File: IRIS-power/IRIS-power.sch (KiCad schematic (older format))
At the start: 11 parts, among them J101 Powerpole, J102 PJ-047AH, U101 TVS1400DRV, U102 TVS1400DRV

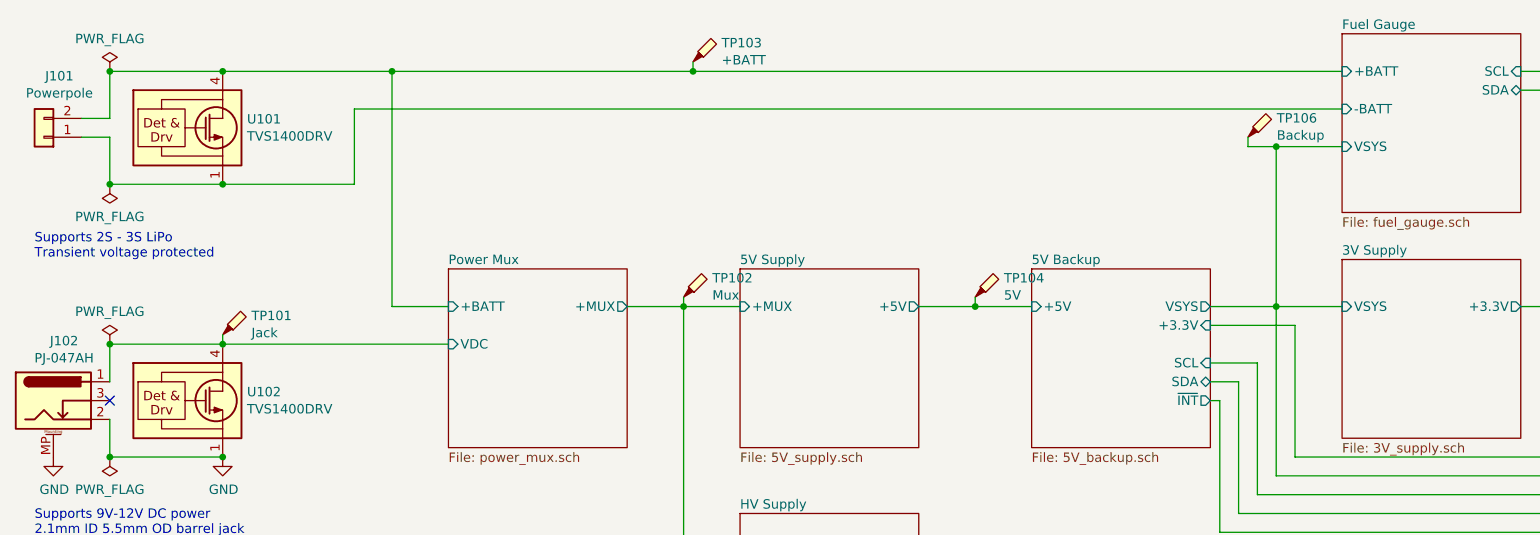
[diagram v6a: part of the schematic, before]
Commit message: Updated layout
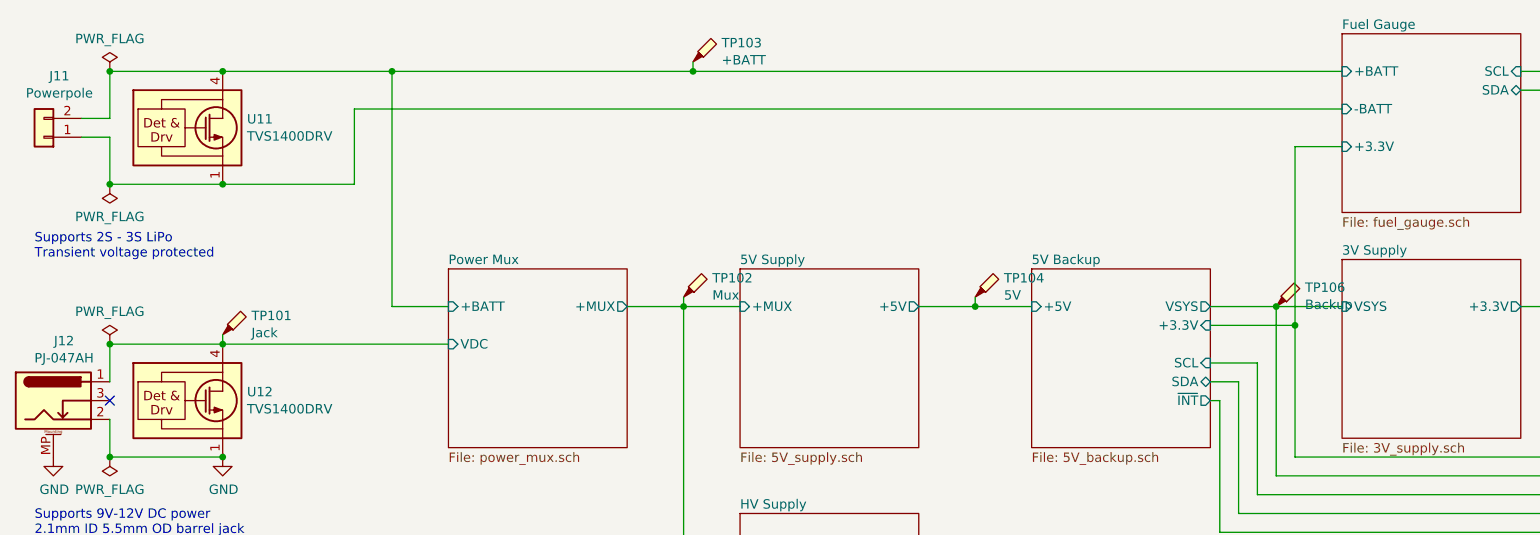
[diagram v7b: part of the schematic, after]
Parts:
- U11: renamed from U101; footprint Package_SON:WSON-6-1EP_2x2mm_P0.65mm_EP1x1.6mm -> star-common-lib:WSON-6-1EP_2x2mm_Hand_Solder
- U12: renamed from U102; footprint Package_SON:WSON-6-1EP_2x2mm_P0.65mm_EP1x1.6mm -> star-common-lib:WSON-6-1EP_2x2mm_Hand_Solder
- renumbered J101 to J11, J102 to J12
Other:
- moved on the sheet: TP106
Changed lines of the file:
@@
 F4 "SCL" I R 8800 2300 50
 F5 "SDA" B R 8800 2400 50
-F6 "VSYS" I L 7850 2700 50
+F6 "+3.3V" I L 7850 2700 50
 $EndSheet
 $Sheet
@@
 	8800 3550 9000 3550
 $Comp
-L Connector_Generic:Conn_01x02 J101
+L Connector_Generic:Conn_01x02 J11
 U 1 1 5F2F210B
 P 950 2650
-AR Path="/5F2F210B" Ref="J101"  Part="1"
+AR Path="/5F2F210B" Ref="J11"  Part="1"
 AR Path="/5F38FD4F/5F2F210B" Ref="J?"  Part="1"
-F 0 "J101" H 868 2325 50  0000 C CNN
+F 0 "J11" H 868 2325 50  0000 C CNN
 F 1 "Powerpole" H 868 2416 50  0000 C CNN
 F 2 "star-common-lib:Powerpole_1336G1" H 950 2650 50  0001 C CNN
@@
 $EndComp
 $Comp
-L Connector:Barrel_Jack_Switch_MountingPin J102
+L Connector:Barrel_Jack_Switch_MountingPin J12
 U 1 1 5F2F2122
 P 1000 4050
-AR Path="/5F2F2122" Ref="J102"  Part="1"
+AR Path="/5F2F2122" Ref="J12"  Part="1"
 AR Path="/5F38FD4F/5F2F2122" Ref="J?"  Part="1"
-F 0 "J102" H 1057 4367 50  0000 C CNN
+F 0 "J12" H 1057 4367 50  0000 C CNN
 F 1 "PJ-047AH" H 1057 4276 50  0000 C CNN
 F 2 "star-common-lib:CUI_PJ-047AH" H 1050 4010 50  0001 C CNN
@@
 P 1900 2600
 AR Path="/5F38FD4F/5F2F2145" Ref="U?"  Part="1"
-AR Path="/5F2F2145" Ref="U101"  Part="1"
-F 0 "U101" H 2029 2646 50  0000 L CNN
+AR Path="/5F2F2145" Ref="U11"  Part="1"
+F 0 "U11" H 2029 2646 50  0000 L CNN
 F 1 "TVS1400DRV" H 2029 2555 50  0000 L CNN
-F 2 "Package_SON:WSON-6-1EP_2x2mm_P0.65mm_EP1x1.6mm" H 2100 2250 50  0001 C CNN
+F 2 "star-common-lib:WSON-6-1EP_2x2mm_Hand_Solder" H 2100 2250 50  0001 C CNN
 F 3 "http://www.ti.com/lit/ds/symlink/tvs1400.pdf" H 1800 2600 50  0001 C CNN
 	1    1900 2600
@@
 P 1900 4050
 AR Path="/5F38FD4F/5F2F214D" Ref="U?"  Part="1"
-AR Path="/5F2F214D" Ref="U102"  Part="1"
-F 0 "U102" H 2029 4096 50  0000 L CNN
+AR Path="/5F2F214D" Ref="U12"  Part="1"
+F 0 "U12" H 2029 4096 50  0000 L CNN
 F 1 "TVS1400DRV" H 2029 4005 50  0000 L CNN
-F 2 "Package_SON:WSON-6-1EP_2x2mm_P0.65mm_EP1x1.6mm" H 2100 3700 50  0001 C CNN
+F 2 "star-common-lib:WSON-6-1EP_2x2mm_Hand_Solder" H 2100 3700 50  0001 C CNN
 F 3 "http://www.ti.com/lit/ds/symlink/tvs1400.pdf" H 1800 4050 50  0001 C CNN
 	1    1900 4050
@@
 	9400 2300 9400 4550
 Wire Wire Line
-	7500 2700 7850 2700
-Wire Wire Line
 	7150 3550 7500 3550
 Wire Wire Line
@@
 Wire Wire Line
 	7150 3950 7300 3950
-Wire Wire Line
-	7500 2700 7500 3550
 Connection ~ 7500 3550
 Wire Wire Line
@@
 L Connector:TestPoint_Probe TP106
 U 1 1 5F31F80A
-P 7350 2650
-F 0 "TP106" H 7503 2751 50  0000 L CNN
-F 1 "Backup" H 7503 2660 50  0000 L CNN
-F 2 "TestPoint:TestPoint_Keystone_5000-5004_Miniature" H 7550 2650 50  0001 C CNN
-F 3 "~" H 7550 2650 50  0001 C CNN
-	1    7350 2650
+P 7500 3550
+F 0 "TP106" H 7653 3651 50  0000 L CNN
+F 1 "Backup" H 7653 3560 50  0000 L CNN
+F 2 "TestPoint:TestPoint_Keystone_5000-5004_Miniature" H 7700 3550 50  0001 C CNN
+F 3 "~" H 7700 3550 50  0001 C CNN
+	1    7500 3550
 	1    0    0    -1
 $EndComp
@@
 	4400 2300 7850 2300
 Wire Wire Line
-	7500 2700 7350 2700
-Wire Wire Line
-	7350 2700 7350 2650
-Connection ~ 7500 2700
-Wire Wire Line
 	9000 3550 9700 3550
 Wire Wire Line
@@
 Wire Wire Line
 	1900 3750 1900 3700
+Wire Wire Line
+	7600 3650 7600 2700
+Connection ~ 7600 3650
+Wire Wire Line
+	7600 2700 7850 2700
 $EndSCHEMATC

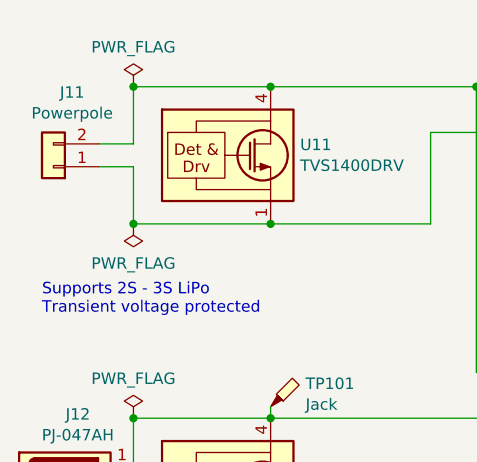
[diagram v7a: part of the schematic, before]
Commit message: Updated 3D models
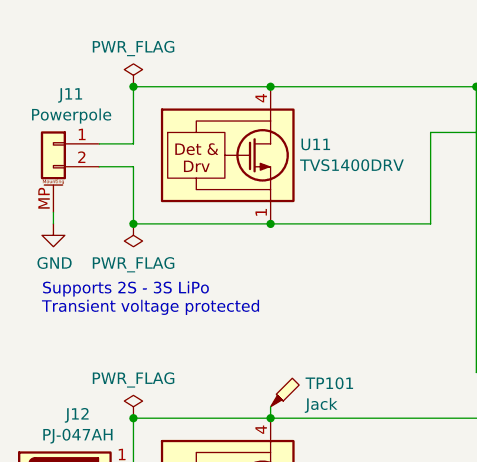
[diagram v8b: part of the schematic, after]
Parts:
- removed J11: Powerpole, star-common-lib:Powerpole_1336G1, symbol Connector_Generic:Conn_01x02
- added J11: Powerpole, star-common-lib:Powerpole_1336G1, symbol Connector_Generic_MountingPin:Conn_01x02_MountingPin
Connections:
- net Fuel Gauge/+BATT: now also J11.1 (Pin_1)
- net Fuel Gauge/-BATT: now also J11.2 (Pin_2)
- net GND: now also J11.MP (MountPin)
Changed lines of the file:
@@
 Wire Wire Line
 	8800 3550 9000 3550
-$Comp
-L Connector_Generic:Conn_01x02 J11
-U 1 1 5F2F210B
-P 950 2650
-AR Path="/5F2F210B" Ref="J11"  Part="1"
-AR Path="/5F38FD4F/5F2F210B" Ref="J?"  Part="1"
-F 0 "J11" H 868 2325 50  0000 C CNN
-F 1 "Powerpole" H 868 2416 50  0000 C CNN
-F 2 "star-common-lib:Powerpole_1336G1" H 950 2650 50  0001 C CNN
-F 3 "~" H 950 2650 50  0001 C CNN
-	1    950  2650
-	-1   0    0    1
-$EndComp
 Wire Wire Line
 	1150 2550 1300 2550
@@
 Wire Wire Line
 	7600 2700 7850 2700
+$Comp
+L Connector_Generic_MountingPin:Conn_01x02_MountingPin J11
+U 1 1 5F44C754
+P 950 2550
+F 0 "J11" H 872 2767 50  0000 C CNN
+F 1 "Powerpole" H 872 2676 50  0000 C CNN
+F 2 "star-common-lib:Powerpole_1336G1" H 950 2550 50  0001 C CNN
+F 3 "~" H 950 2550 50  0001 C CNN
+	1    950  2550
+	-1   0    0    -1
+$EndComp
+Wire Wire Line
+	950  2850 950  2900
+$Comp
+L power:GND #PWR0106
+U 1 1 5F44E82C
+P 950 2900
+AR Path="/5F44E82C" Ref="#PWR0106"  Part="1"
+AR Path="/5F38FD4F/5F44E82C" Ref="#PWR?"  Part="1"
+F 0 "#PWR0106" H 950 2650 50  0001 C CNN
+F 1 "GND" H 955 2727 50  0000 C CNN
+F 2 "" H 950 2900 50  0001 C CNN
+F 3 "" H 950 2900 50  0001 C CNN
+	1    950  2900
+	1    0    0    -1
+$EndComp
 $EndSCHEMATC
